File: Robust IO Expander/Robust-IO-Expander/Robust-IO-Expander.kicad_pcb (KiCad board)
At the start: 2 copper layers, 174.5 x 74.4 mm, 61 parts, among them J1 Input Headers, J10 Right SPI In, J11 SPI Inputs, J12 Power Input, J2 CS Inputs, J3 CS Inputs, J4 SPI Inputs, J5 Input Screw Terminal, J6 Output Screw Terminal, J7 Ouput Headers, J8 Power Input, J9 Left SPI Out, U1 MCP23S17_SS, U10 LTV-847S, U11 AMS1117-3.3, U2 MCP23S17_SS, U3 LTV-847S, U4 LTV-847S, U5 LTV-847S, U6 LTV-847S, U7 LTV-847S, U8 LTV-847S, U9 LTV-847S

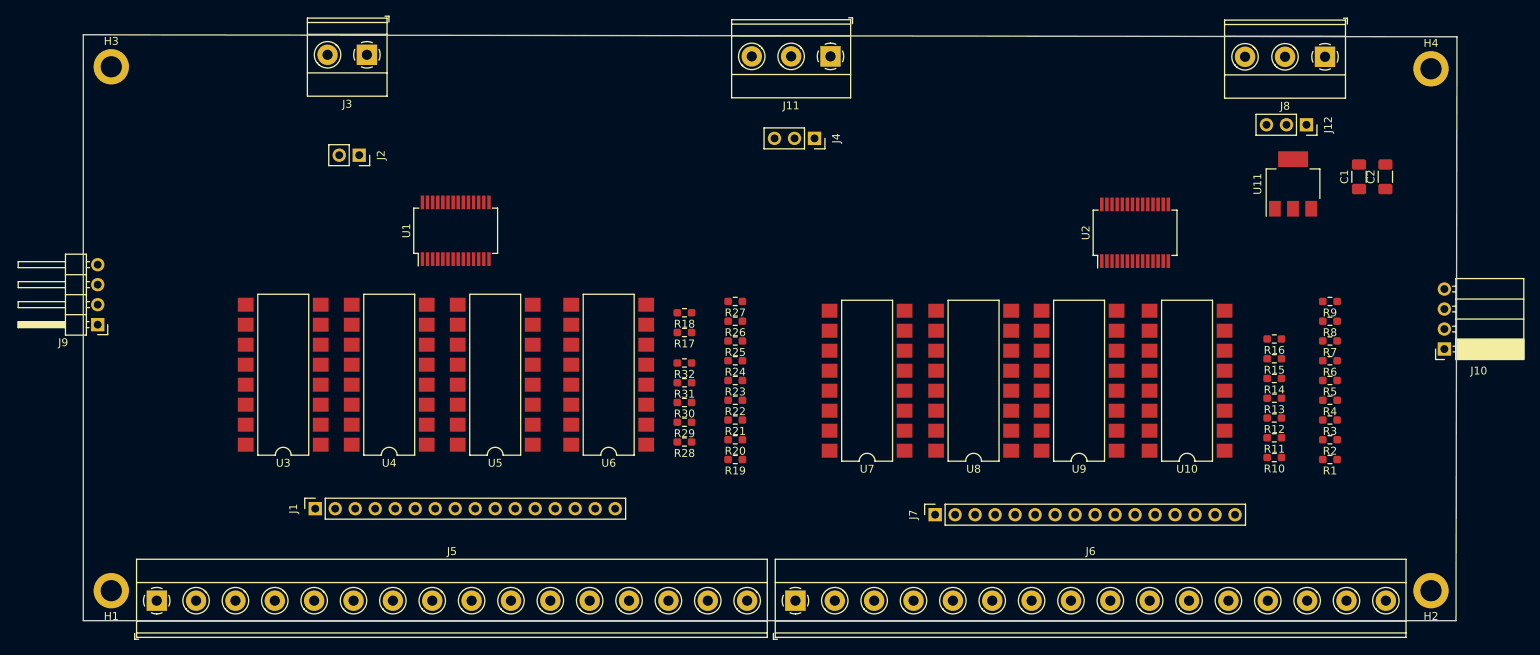
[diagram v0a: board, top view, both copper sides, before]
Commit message: Layout change
AD 15/10/23: Add Screw terminals everywhere
ESD Protection on IO and SPI Inputs
3.3v Regulator for IO power
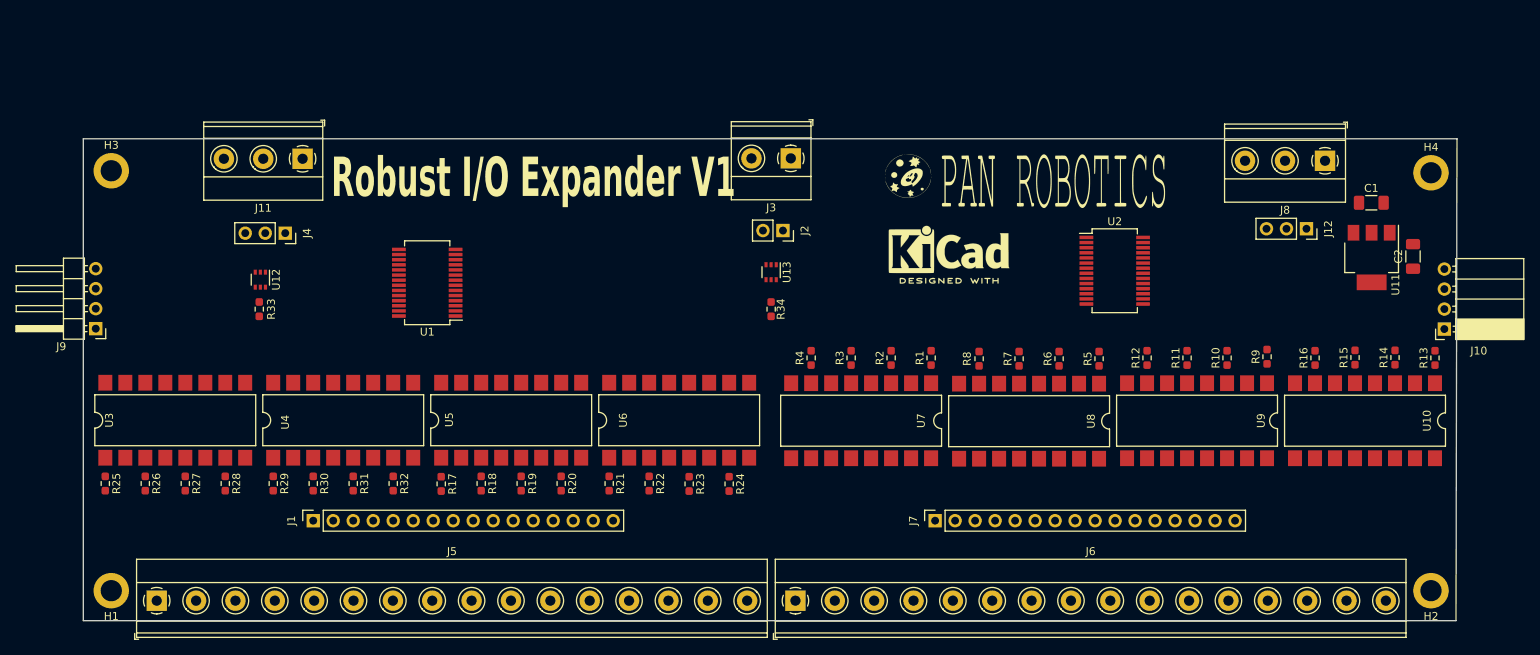
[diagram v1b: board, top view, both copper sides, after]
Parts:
- added G***: LOGO, Logos:Pan-Robotics-Logo7, F.Cu at (172.5, 78.5)
- added R33: 10K, Resistor_SMD:R_0603_1608Metric_Pad0.98x0.95mm_HandSolder, F.Cu at (75.2, 94.8)
- added R34: 10K, Resistor_SMD:R_0603_1608Metric_Pad0.98x0.95mm_HandSolder, F.Cu at (140.2, 94.8)
- added REF**: KiCad-Logo2_6mm_SilkScreen, Symbol:KiCad-Logo2_6mm_SilkScreen, F.Cu at (162.8, 87.2)
- added U12: NUP4202, Package_TO_SOT_SMD:SOT-363_SC-70-6, F.Cu at (75.3, 91.0)
- added U13: NUP4202, Package_TO_SOT_SMD:SOT-363_SC-70-6, F.Cu at (140.2, 90.1)
- moved R25 82.0 mm to (55.6, 116.9), turned to -90 degrees
- moved R26 77.7 mm to (60.7, 116.9), turned to -90 degrees
- moved R27 73.6 mm to (65.8, 116.9), turned to -90 degrees
- moved J11 68.3 mm to (80.7, 75.7)
- moved J4 68.3 mm to (78.5, 85.1)
- moved R4 66.1 mm to (145.3, 101.0), turned to 90 degrees
- moved R3 61.3 mm to (150.4, 101.0), turned to 90 degrees
- moved R28 58.6 mm to (70.9, 116.9), turned to -90 degrees
- moved R2 56.7 mm to (155.4, 101.0), turned to 90 degrees
- moved J3 55.4 mm to (142.7, 75.6)
- moved J2 54.7 mm to (141.7, 84.8)
- moved R29 52.8 mm to (77.0, 116.9), turned to -90 degrees
- moved R1 52.3 mm to (160.5, 101.0), turned to 90 degrees
- moved R30 48.3 mm to (82.0, 116.9), turned to -90 degrees
- moved R8 44.8 mm to (166.6, 101.1), turned to 90 degrees
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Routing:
- added copper zone on In1.Cu, net +3.3V
- added copper zone on In2.Cu, net GND
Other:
- board size 174.5 x 74.4 mm -> 174.5 x 61.2 mm
- copper layers 2 -> 4
- board text added: "Robust I/O Expander V1"

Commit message: Design Complete
AD 10/12/23:
Design Finalised
BOM Created
Gerber and POS Files Generate
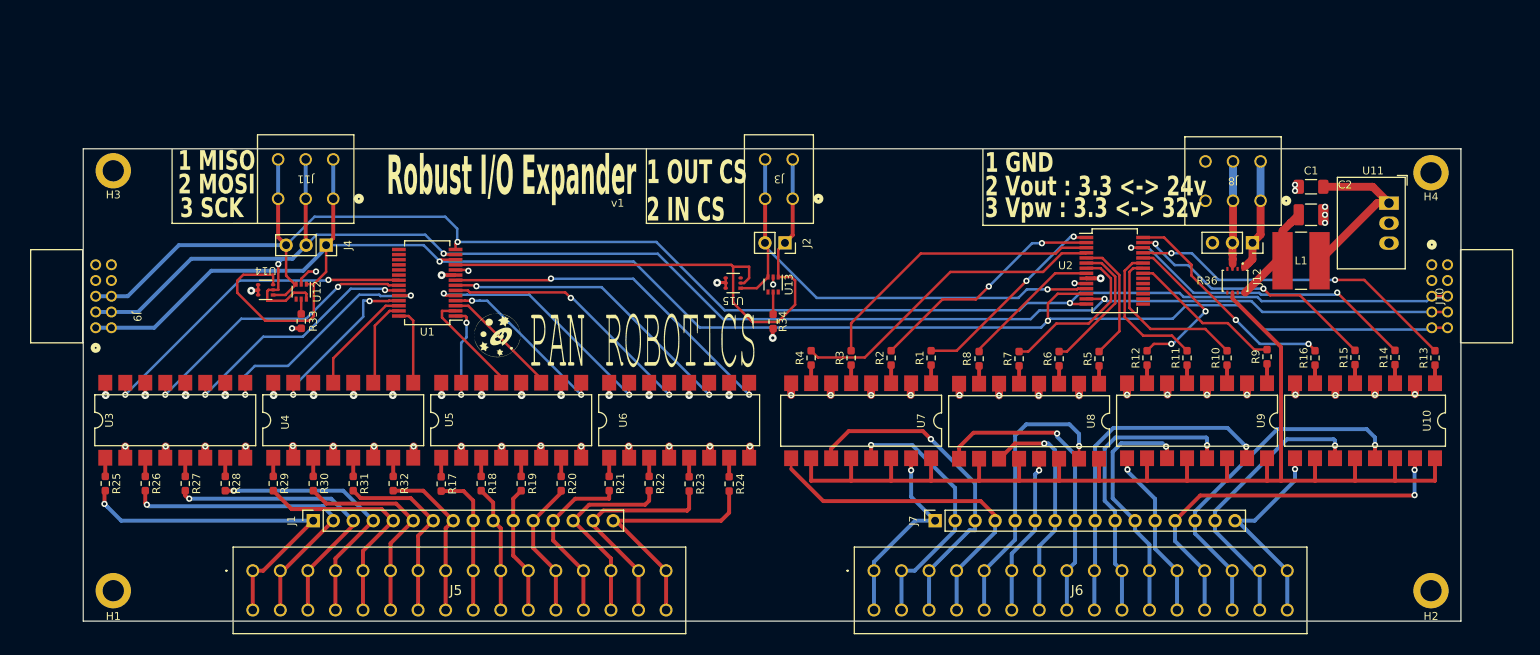
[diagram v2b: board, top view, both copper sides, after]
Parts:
- removed REF**: KiCad-Logo2_6mm_SilkScreen, Symbol:KiCad-Logo2_6mm_SilkScreen
- added L1: 10uH, SRR6038_100Y footprint:IND_BOURNS_SRR6038, F.Cu at (207.5, 88.6)
- added R36: RB061US-30TR, RB061US_30TR footprints:DIO_RB061U_ROM, F.Cu at (199.1, 91.2)
- added U14: BZX84C5V1TS-7-F, footprints:SOT-363_DIO, F.Cu at (76.0, 92.3)
- added U15: BZX84C5V1TS-7-F, footprints:SOT-363_DIO, F.Cu at (135.4, 91.5)
- C1: footprint Capacitor_SMD:C_1206_3216Metric_Pad1.33x1.80mm_HandSolder -> Capacitor_SMD:C_1210_3225Metric_Pad1.33x2.70mm_HandSolder
- C2: value 22uF -> 4.7uF
- J10: footprint Connector_PinSocket_2.54mm:PinSocket_1x04_P2.54mm_Horizontal -> LS2_105_01_F_D_RA2 footprint:CONN_LS2-105-01-X-D-RA2_SAI
- J11: value SPI Inputs -> SPI Terminal; footprint TerminalBlock_Phoenix:TerminalBlock_Phoenix_MKDS-1,5-3_1x03_P5.00mm_Horizontal -> 1862055 footprint:CONN_1862055
- J3: value CS Inputs -> CS Terminal; footprint TerminalBlock_Phoenix:TerminalBlock_Phoenix_MKDS-1,5-2_1x02_P5.00mm_Horizontal -> 1862042 footprint:CONN_1862042
- J5: value Input Screw Terminal -> Input Terminal; footprint TerminalBlock_Phoenix:TerminalBlock_Phoenix_MKDS-1,5-16_1x16_P5.00mm_Horizontal -> 1862262 footprint:1862262
- J6: value Output Screw Terminal -> Output Terminal; footprint TerminalBlock_Phoenix:TerminalBlock_Phoenix_MKDS-1,5-16_1x16_P5.00mm_Horizontal -> 1862262 footprint:1862262
- J8: footprint TerminalBlock_Phoenix:TerminalBlock_Phoenix_MKDS-1,5-3-5.08_1x03_P5.08mm_Horizontal -> 1862055 footprint:CONN_1862055
- J9: footprint Connector_PinHeader_2.54mm:PinHeader_1x04_P2.54mm_Horizontal -> LS2_105_01_F_D_RA1 footprint:CONN_LS2-105-01-X-D-RA1_SAI
- U11: value AMS1117-3.3 -> R-78B3.3-2.0; footprint Package_TO_SOT_SMD:SOT-223-3_TabPin2 -> Converter_DCDC:Converter_DCDC_RECOM_R-78B-2.0_THT
- moved G*** 56.0 mm to (120.3, 98.7)
- moved C2 15.7 mm to (208.8, 79.2), turned to 180 degrees
- moved J8 15.2 mm to (195.4, 76.0)
- moved J5 12.8 mm to (74.4, 128.0)
- moved J6 10.7 mm to (153.3, 128.0)
- moved J10 8.32 mm to (224.1, 89.2), turned to 90 degrees
- moved C1 7.81 mm to (208.8, 82.8)
- moved U11 7.26 mm to (218.7, 81.3)
- moved J12 7.08 mm to (201.4, 86.4)
- moved R33 5.55 mm to (80.5, 96.3)
- moved U12 5.41 mm to (80.5, 92.6)
- moved J4 5.41 mm to (83.7, 86.7)
- moved J3 3.26 mm to (139.4, 75.8)
- moved J11 3.11 mm to (77.6, 75.8)
- moved U13 1.59 mm to (140.5, 91.7)
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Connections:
- C2 pad 1: +3.3V -> Net-(U11-IN)
- J10 pad 1: SCK -> unconnected-(J10-Pad1)
- J10 pad 2: MOSI -> unconnected-(J10-Pad2)
- J10 pad 3: MISO -> GND
- J11 pad 2: MOSI -> SCK
- J11 pad 3: MISO -> MOSI
- J12 pad 1: VCC -> Net-(J12-Pin_1)
- J12 pad 2: +24V -> Net-(J12-Pin_2)
- J3 pad 2: OutCS -> InCS
- J8 pad 1: VCC -> Net-(J12-Pin_1)
- J8 pad 2: +24V -> Net-(J12-Pin_1)
- J8 pad 3: GND -> Net-(J12-Pin_2)
- J9 pad 2: MOSI -> SCK
- J9 pad 3: MISO -> MOSI
- J9 pad 4: GND -> MOSI
- U11 pad 1: GND -> Net-(U11-IN)
- U11 pad 2: +3.3V -> GND
- U11 pad 3: VCC -> +3.3V
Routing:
- net SCK: track 0.00 -> 234.0 mm, vias 0 -> 2
- net MOSI: track 0.00 -> 209.8 mm, vias 0 -> 3
- net MISO: track 0.00 -> 207.1 mm, vias 0 -> 2
- net +24V: track 0.00 -> 151.1 mm
- net InCS: track 0.00 -> 75.6 mm
- net OutCS: track 0.00 -> 63.6 mm, vias 0 -> 1
- net GND: track 0.00 -> 62.0 mm, vias 0 -> 43
- net EOUT12: track 0.00 -> 49.5 mm, vias 0 -> 2
- net IN15: track 0.00 -> 45.0 mm, vias 0 -> 2
- net EOUT13: track 0.00 -> 44.7 mm, vias 0 -> 1
- net EIN0: track 0.00 -> 44.4 mm, vias 0 -> 1
- net EOUT3: track 0.00 -> 43.8 mm
- net EOUT8: track 0.00 -> 43.5 mm, vias 0 -> 1
- net IN0: track 0.00 -> 42.3 mm, vias 0 -> 2
- net Out12: track 0.00 -> 42.2 mm, vias 0 -> 2
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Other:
- board size 174.5 x 61.2 mm -> 175 x 60 mm
- board text added: "1 GND"
- board text added: "1 MISO"
- board text added: "1 OUT CS"
- board text added: "2 IN CS"
- board text added: "2 MOSI"
- board text added: "2 Vout : 3.3 <-> 24v"
- board text added: "3 SCK"
- board text added: "3 Vpw : 3.3 <-> 32v"
- board text added: "Robust I/O Expander"
- board text added: "v1"
- board text removed: "Robust I/O Expander V1"

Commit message: Updates
AD 12/11/23
1K Resistors inserted for 200R
0603 components Error correct to 0805
Post DFM Analysis Changes
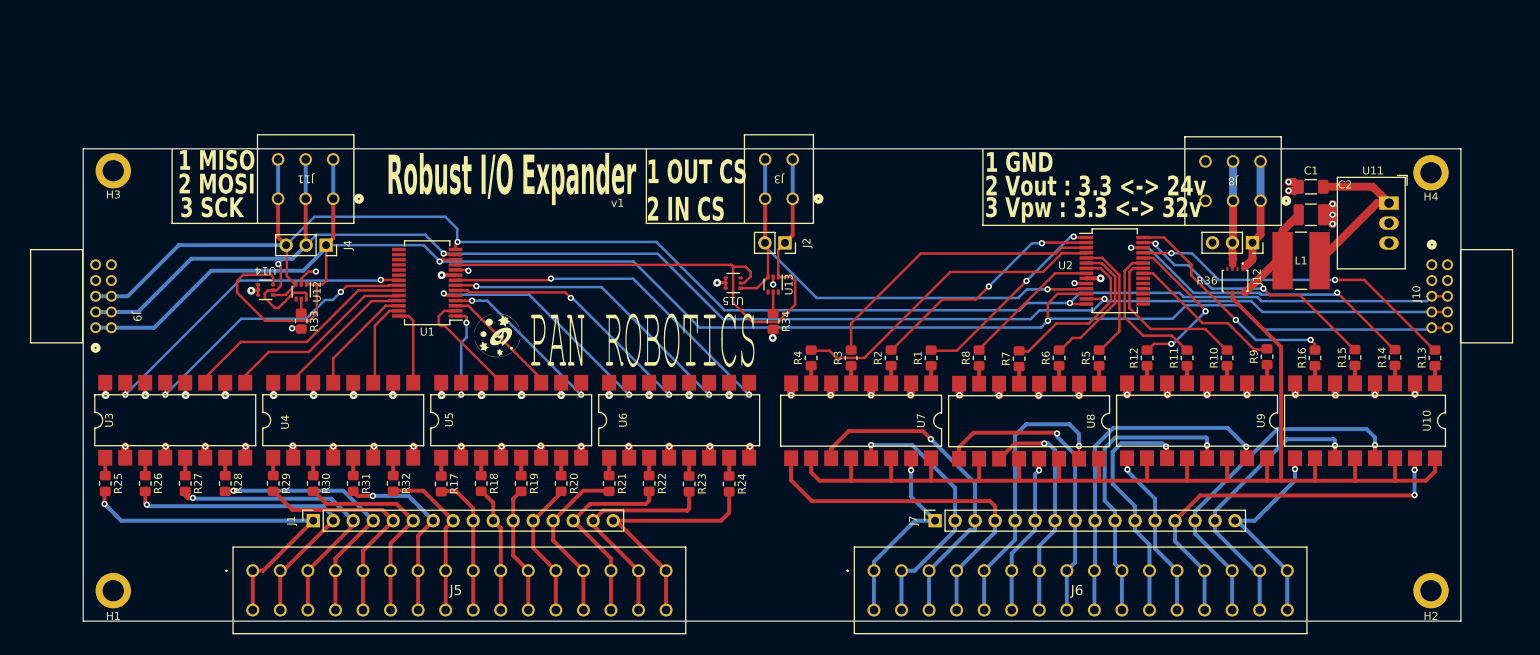
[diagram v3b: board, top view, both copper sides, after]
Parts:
- R1, R10, R11, R12, R13, R14, R15, R16, R17, R18, R19, R2, R20, R21, R22, R23, R24, R25, R26, R27, R28, R29, R3, R30, R31, R32, R4, R5, R6, R7, R8, R9: value 200R -> 1K; footprint Resistor_SMD:R_0603_1608Metric_Pad0.98x0.95mm_HandSolder -> Resistor_SMD:R_0805_2012Metric_Pad1.20x1.40mm_HandSolder
- R33, R34: footprint Resistor_SMD:R_0603_1608Metric_Pad0.98x0.95mm_HandSolder -> Resistor_SMD:R_0805_2012Metric_Pad1.20x1.40mm_HandSolder
- moved R5 0.10 mm to (181.9, 101.0)
- moved R6 0.10 mm to (176.8, 101.0)
- moved R8 0.10 mm to (166.6, 101.0)
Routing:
- net GND: track 62.0 -> 71.4 mm
- net IN3: track 30.9 -> 24.6 mm, vias 2 -> 0
- net IN4: track 21.7 -> 18.0 mm, vias 2 -> 0
- net IN2: track 31.8 -> 29.8 mm, vias 2 -> 0
- net EOUT3: track 43.8 -> 45.3 mm
- net +24V: track 151.1 -> 149.8 mm
- net MOSI: track 209.8 -> 211.0 mm
- net SCK: track 234.0 -> 235.1 mm
- net EIN12: track 22.2 -> 21.6 mm
- net EIN8: track 18.5 -> 17.9 mm
- net EIN6: track 23.9 -> 23.8 mm, vias 0 -> 1
